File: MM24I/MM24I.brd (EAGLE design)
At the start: 125.7 x 62.2 mm, 42 parts, among them IC1 SN74LVC2G17DBVR, IC2 SN74LVC14APWR, U1 SN74LVCH16374ADGGR, U2 SN74LVCH16374ADGGR, U3 CY14B104M, U4 SN74AHCT16373DGGR, U5 TLV803SDBZ

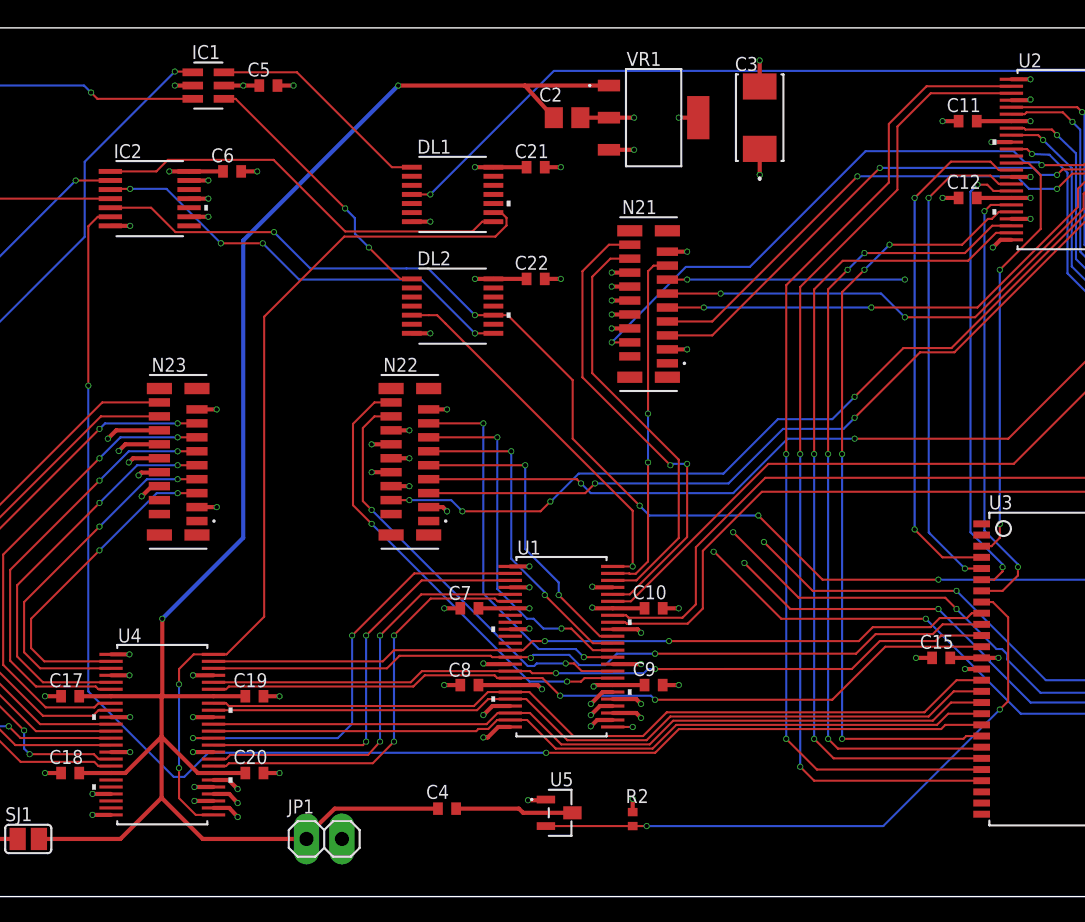
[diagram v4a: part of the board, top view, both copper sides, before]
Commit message: Rework MM24I voltage supervisor
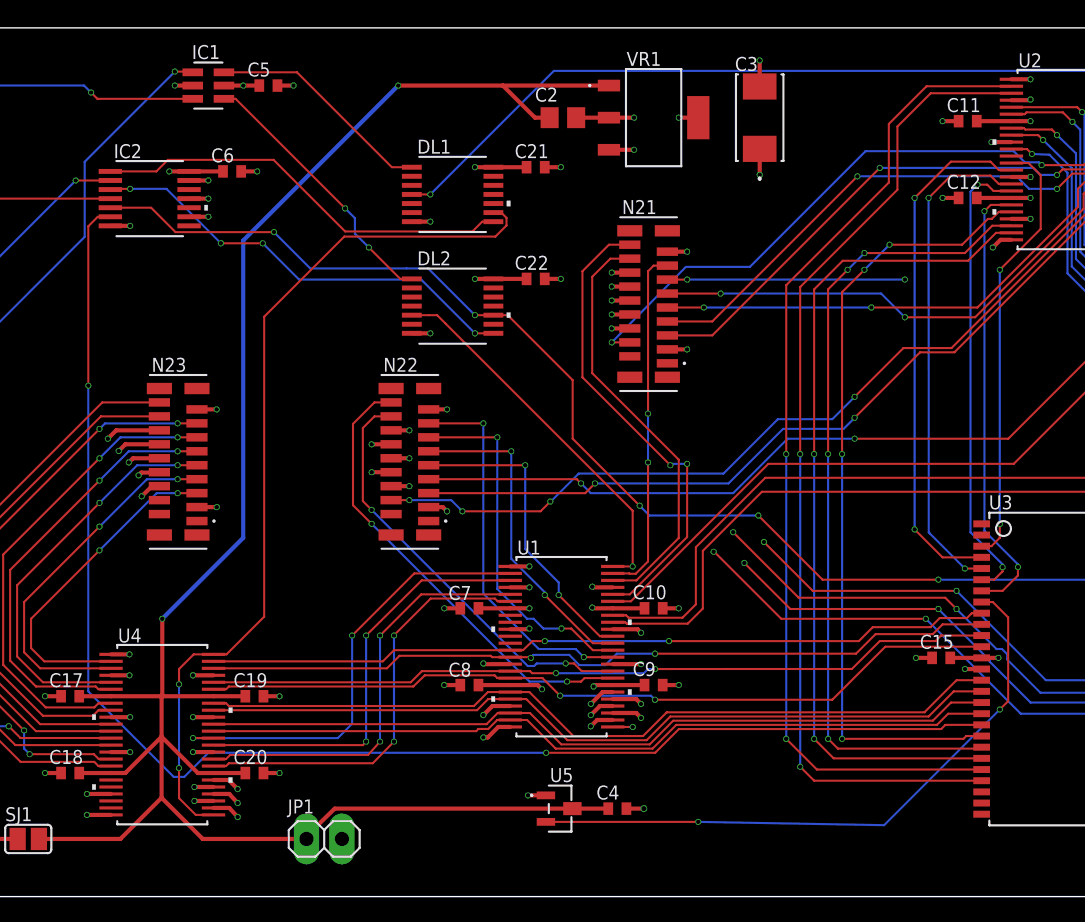
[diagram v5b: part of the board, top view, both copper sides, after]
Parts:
- removed R2: 10k, rcl:R0402
- C14: value 0.1 UF -> 0.01 UF
- U5: value TLV803SDBZ -> TLV809EA46DBZR
- moved C4 12.2 mm to (64.2, 6.30)
- moved C2 0.30 mm to (60.3, 55.8)
- moved U5 0.30 mm to (60.1, 6.30)
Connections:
- removed net N$1: C4.2, U5.3
- net !POWER-OK: no longer R2.1
- net +5V: now also U5.3
- net GND: now also C4.2
- net VCC: no longer R2.2
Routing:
- net +5V: track 134.3 -> 147.7 mm
- net N$1: track 8.46 -> 0.00 mm
- net GND: track 210.0 -> 212.3 mm, vias 112 -> 113
- net VCC: track 56.7 -> 55.7 mm, vias 17 -> 16

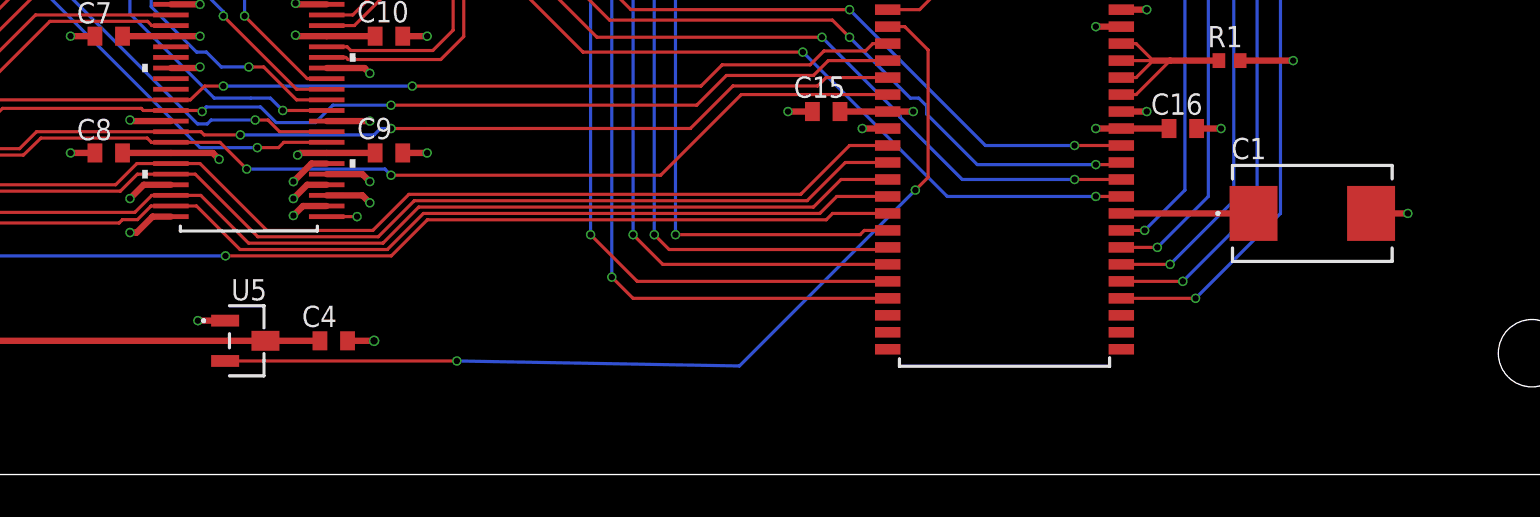
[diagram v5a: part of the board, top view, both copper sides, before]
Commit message: Disable thermals on pours to work around EAGLE bug
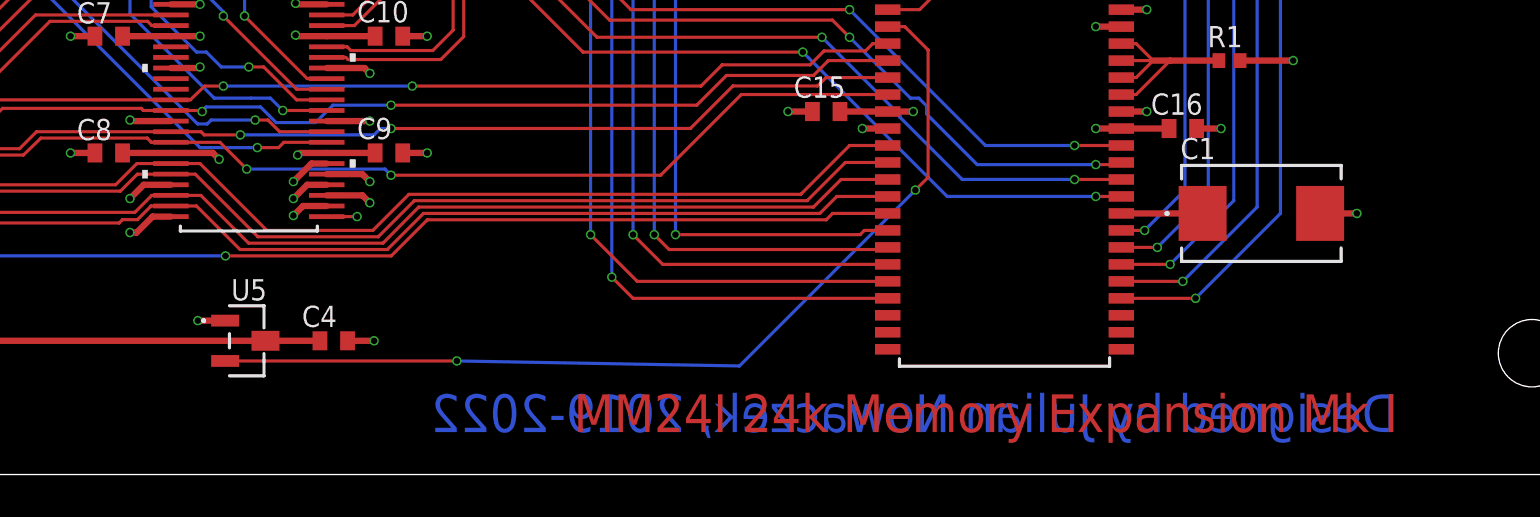
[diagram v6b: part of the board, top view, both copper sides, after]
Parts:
- moved C1 2.40 mm to (107.9, 12.3)
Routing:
- net VCAP: track 6.23 -> 3.83 mm
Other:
- board text added: "Designed by Julian Nowaczek, 2019-2022"
- board text added: "MM24I 24k Memory Expansion Mk I"
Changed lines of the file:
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@@
 <layer number="28" name="bValues" color="7" fill="1" visible="yes" active="yes"/>
 <layer number="29" name="tStop" color="7" fill="3" visible="yes" active="yes"/>
-<layer number="30" name="bStop" color="7" fill="6" visible="no" active="yes"/>
+<layer number="30" name="bStop" color="7" fill="6" visible="yes" active="yes"/>
 <layer number="31" name="tCream" color="7" fill="4" visible="no" active="yes"/>
 <layer number="32" name="bCream" color="7" fill="5" visible="no" active="yes"/>
@@
 <text x="40.6" y="2.2" size="1" layer="51" ratio="15" align="top-left">+5</text>
 <text x="45.8" y="2.2" size="1" layer="51" ratio="15" align="top-right">GND</text>
+<text x="114.3254" y="2" size="1.778" layer="29" ratio="15" align="bottom-right">MM24I 24k Memory Expansion Mk I</text>
+<text x="114.3254" y="2" size="1.778" layer="30" ratio="15" rot="MR0">Designed by Julian Nowaczek, 2019-2022</text>
+<text x="114.3254" y="2" size="1.778" layer="1" ratio="15" align="bottom-right">MM24I 24k Memory Expansion Mk I</text>
+<text x="114.3254" y="2" size="1.778" layer="16" ratio="15" rot="MR0">Designed by Julian Nowaczek, 2019-2022</text>
 </plain>
 <attributes>
@@
 </class>
 </classes>
-<designrules name="jlcpcb-4layers">
-<description language="en">&lt;b&gt;JLCPCB design rules (4 layers)&lt;/b&gt;
+<designrules name="jlcpcb-2layers *">
+<description language="en">&lt;b&gt;JLCPCB design rules (2 layers)&lt;/b&gt;
 &lt;ul&gt;
-&lt;li&gt;Board thickness: 1.2mm&lt;/li&gt;
+&lt;li&gt;Board thickness: 1.6mm&lt;/li&gt;
 &lt;li&gt;Copper weight: 1oz (35um)&lt;/li&gt;
 &lt;li&gt;Note: annular ring aren't minimal&lt;/li&gt;
 &lt;/ul&gt;</description>
 <param name="layerSetup" value="(1+2*15+16)"/>
-<param name="mtCopper" value="0.035mm 0.0175mm 0.035mm 0.035mm 0.035mm 0.035mm 0.035mm 0.035mm 0.035mm 0.035mm 0.035mm 0.035mm 0.035mm 0.035mm 0.0175mm 0.035mm"/>
-<param name="mtIsolate" value="0.2mm 0.665mm 0.2mm 0.15mm 0.2mm 0.15mm 0.2mm 0.15mm 0.2mm 0.15mm 0.2mm 0.15mm 0.2mm 0.15mm 0.2mm"/>
+<param name="mtCopper" value="0.035mm 0.035mm 0.035mm 0.035mm 0.035mm 0.035mm 0.035mm 0.035mm 0.035mm 0.035mm 0.035mm 0.035mm 0.035mm 0.035mm 0.035mm 0.035mm"/>
+<param name="mtIsolate" value="0.11mm 0.8mm 0.2mm 0.15mm 0.2mm 0.15mm 0.2mm 0.15mm 0.2mm 0.15mm 0.2mm 0.15mm 0.2mm 0.15mm 0.11mm"/>
 <param name="mdWireWire" value="5mil"/>
 <param name="mdWirePad" value="5mil"/>
@@
 <param name="srMinRoundness" value="0mil"/>
 <param name="srMaxRoundness" value="0mil"/>
-<param name="slThermalIsolate" value="10mil"/>
+<param name="slThermalIsolate" value="0mil"/>
 <param name="slThermalsForVias" value="0"/>
 <param name="dpMaxLengthDifference" value="10mm"/>
@@
 </groups>
 <elements>
-<element name="C1" library="MM24I" package="CAPCP7343X430N" value="100UF" x="110.3" y="12.3" smashed="yes">
-<attribute name="CAPACITANCETOLERANCE" value="±20%" x="152.21" y="-19.45" size="1.778" layer="27" display="off"/>
-<attribute name="MPN" value="NOJD107M010RWJ" x="152.21" y="-19.45" size="1.778" layer="27" display="off"/>
-<attribute name="NAME" x="106.4856" y="14.857" size="1" layer="25" font="vector" ratio="15" rot="SR0"/>
-<attribute name="SUPPLIER" value="AVX" x="152.21" y="-19.45" size="1.778" layer="27" display="off"/>
-<attribute name="VOLTAGERATING" value="10V" x="152.21" y="-19.45" size="1.778" layer="27" display="off"/>
+<element name="C1" library="MM24I" package="CAPCP7343X430N" value="100UF" x="107.9" y="12.3" smashed="yes">
+<attribute name="CAPACITANCETOLERANCE" value="±20%" x="149.81" y="-19.45" size="1.778" layer="27" display="off"/>
+<attribute name="MPN" value="NOJD107M010RWJ" x="149.81" y="-19.45" size="1.778" layer="27" display="off"/>
+<attribute name="NAME" x="104.0856" y="14.857" size="1" layer="25" font="vector" ratio="15" rot="SR0"/>
+<attribute name="SUPPLIER" value="AVX" x="149.81" y="-19.45" size="1.778" layer="27" display="off"/>
+<attribute name="VOLTAGERATING" value="10V" x="149.81" y="-19.45" size="1.778" layer="27" display="off"/>
 </element>
 <element name="N20" library="MM24I" package="CON18_1X18_DUTB_HRS" value="FH12-18S-0.5SV(55)" x="105" y="38.2" smashed="yes" rot="R270">
@@
 <signals>
 <signal name="GND" class="1">
-<polygon width="0" layer="2">
+<polygon width="0" layer="2" thermals="no">
 <vertex x="0" y="0"/>
 <vertex x="0" y="62.23"/>
@@
 <via x="102.5" y="17.1" extent="1-16" drill="0.3"/>
 <wire x1="101.3022" y1="17.1" x2="102.5" y2="17.1" width="0.3" layer="1"/>
-<via x="114.8" y="12.3" extent="1-16" drill="0.3"/>
-<wire x1="113.0686" y1="12.3" x2="114.8" y2="12.3" width="0.3" layer="1"/>
+<via x="112.4" y="12.3" extent="1-16" drill="0.3"/>
+<wire x1="110.6686" y1="12.3" x2="112.4" y2="12.3" width="0.3" layer="1"/>
 <via x="54.6" y="13" extent="1-16" drill="0.3"/>
 <wire x1="56.5297" y1="13.65" x2="55.25" y2="13.65" width="0.3" layer="1"/>
@@
 <wire x1="54.9163" y1="11.4" x2="54.6" y2="11.4" width="0.3" layer="1"/>
 <wire x1="55.6663" y1="12.15" x2="54.9163" y2="11.4" width="0.3" layer="1"/>
-<contactref element="JP1" pad="2"/>
 <contactref element="C15" pad="2"/>
 <contactref element="C16" pad="2"/>
@@
 <contactref element="C4" pad="2"/>
 <wire x1="64.85" y1="6.3" x2="66.1" y2="6.3" width="0.3" layer="1"/>
-<via x="66.1" y="6.3" extent="1-16" drill="0.35"/>
+<via x="66.1" y="6.3" extent="1-16" drill="0.3"/>
+<contactref element="JP1" pad="2"/>
 </signal>
 <signal name="VCC" class="1">
@@
 <via x="65.4" y="53.5" extent="1-16" drill="0.3"/>
 <wire x1="63.5996" y1="53.5" x2="65.4" y2="53.5" width="0.3" layer="1"/>
-<polygon width="0" layer="15">
+<polygon width="0" layer="15" thermals="no">
 <vertex x="0" y="0"/>
 <vertex x="125.8" y="0"/>
@@
 </signal>
 <signal name="VCAP" class="1">
-<wire x1="107.5314" y1="12.3" x2="101.3022" y2="12.3" width="0.3" layer="1"/>
+<wire x1="105.1314" y1="12.3" x2="101.3022" y2="12.3" width="0.3" layer="1"/>
 <contactref element="C1" pad="1"/>
 <contactref element="U3" pad="36"/>
@@
 </signals>
 <mfgpreviewcolors>
-<mfgpreviewcolor name="soldermaskcolor" color="0xC8AA007F"/>
+<mfgpreviewcolor name="soldermaskcolor" color="0xC8000000"/>
 <mfgpreviewcolor name="silkscreencolor" color="0xFFFFFFFF"/>
 <mfgpreviewcolor name="backgroundcolor" color="0xFF282828"/>
-<mfgpreviewcolor name="coppercolor" color="0xFFFFBF00"/>
+<mfgpreviewcolor name="coppercolor" color="0xFFFFAA00"/>
 <mfgpreviewcolor name="substratecolor" color="0xFF786E46"/>
 </mfgpreviewcolors>
